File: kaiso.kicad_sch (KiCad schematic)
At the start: 413 parts, among them J1 JST_SH_Conn_01x04, J2 Conn_01x04_Pin, J4 Conn_01x02, SW0_0 Mechanical_Switch, SW0_1 Mechanical_Switch, SW0_10 Mechanical_Switch, SW0_11 Mechanical_Switch, SW0_12 Mechanical_Switch, SW0_13 Mechanical_Switch, SW0_14 Mechanical_Switch, SW0_15 Mechanical_Switch, SW0_16 Mechanical_Switch, SW0_17 Mechanical_Switch, SW0_2 Mechanical_Switch, SW0_3 Mechanical_Switch, SW0_4 Mechanical_Switch, SW0_5 Mechanical_Switch, SW0_6 Mechanical_Switch, SW0_7 Mechanical_Switch, SW0_8 Mechanical_Switch, SW0_9 Mechanical_Switch, SW1 SW_SPDT, SW1_0 Mechanical_Switch, SW1_1 Mechanical_Switch, SW1_10 Mechanical_Switch, SW1_11 Mechanical_Switch, SW1_12 Mechanical_Switch, SW1_13 Mechanical_Switch, SW1_15 Mechanical_Switch, SW1_16 Mechanical_Switch, SW1_17 Mechanical_Switch, SW1_2 Mechanical_Switch, SW1_3 Mechanical_Switch, SW1_4 Mechanical_Switch, SW1_5 Mechanical_Switch, SW1_6 Mechanical_Switch, SW1_7 Mechanical_Switch, SW1_8 Mechanical_Switch, SW1_9 Mechanical_Switch, SW2_0 Mechanical_Switch, SW2_1 Mechanical_Switch, SW2_10 Mechanical_Switch, SW2_11 Mechanical_Switch, SW2_12 Mechanical_Switch, SW2_13 Mechanical_Switch, SW2_15 Mechanical_Switch, SW2_16 Mechanical_Switch, SW2_17 Mechanical_Switch, SW2_2 Mechanical_Switch, SW2_3 Mechanical_Switch, SW2_4 Mechanical_Switch, SW2_5 Mechanical_Switch, SW2_6 Mechanical_Switch, SW2_7 Mechanical_Switch, SW2_8 Mechanical_Switch, SW2_9 Mechanical_Switch, SW3_0 Mechanical_Switch, SW3_1 Mechanical_Switch, SW3_10 Mechanical_Switch, SW3_11 Mechanical_Switch, SW3_12 Mechanical_Switch, SW3_15 Mechanical_Switch, SW3_16 Mechanical_Switch, SW3_17 Mechanical_Switch, SW3_2 Mechanical_Switch, SW3_3 Mechanical_Switch, SW3_4 Mechanical_Switch, SW3_5 Mechanical_Switch, SW3_6 Mechanical_Switch, SW3_7 Mechanical_Switch, SW3_8 Mechanical_Switch, SW3_9 Mechanical_Switch, SW4_0 Mechanical_Switch, SW4_1 Mechanical_Switch, SW4_10 Mechanical_Switch, SW4_11 Mechanical_Switch, SW4_12 Mechanical_Switch, SW4_15 Mechanical_Switch, SW4_16 Mechanical_Switch, SW4_17 Mechanical_Switch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

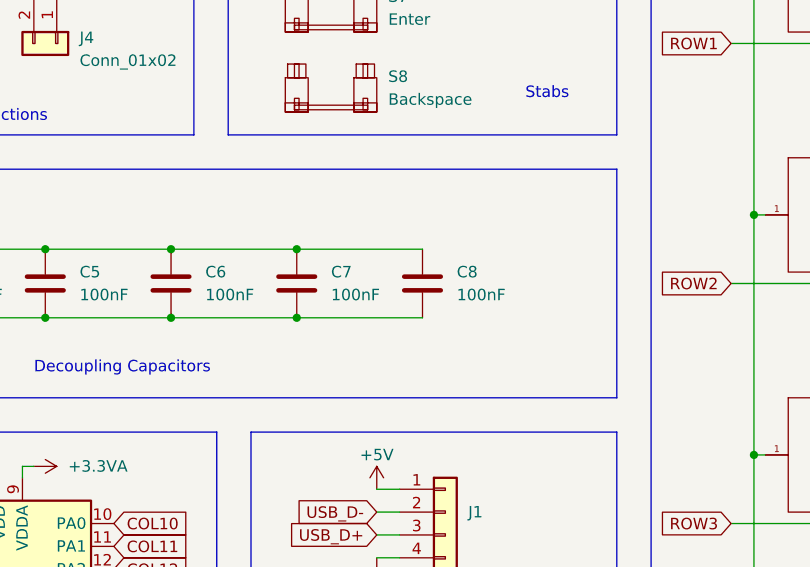
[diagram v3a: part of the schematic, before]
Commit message: started the PCB design
layout complete with switches. still need to figure out how to route it.
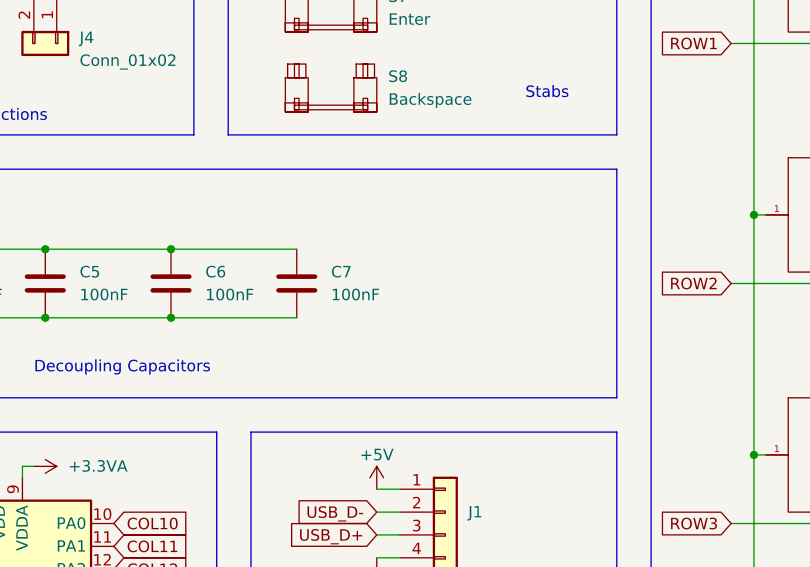
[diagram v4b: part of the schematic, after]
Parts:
- removed C8: 100nF, Capacitor_SMD:C_0402_1005Metric, symbol Device:C
- J1: footprint Connector_JST:JST_SH_BM04B-SRSS-TB_1x04-1MP_P1.00mm_Vertical -> Connector_JST:JST_SH_SM04B-SRSS-TB_1x04-1MP_P1.00mm_Horizontal
- SW1: footprint SW:SW-TH_SK12D07VG3 -> Button_Switch_SMD:SW_SPDT_PCM12
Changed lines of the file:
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@@
   (junction (at 251.46 76.2) (diameter 0) (color 0 0 0 0)
   )
-  (junction (at 81.28 300.99) (diameter 0) (color 0 0 0 0)
-  )
   (junction (at 267.97 163.83) (diameter 0) (color 0 0 0 0)
   )
@@
   (junction (at 135.89 88.9) (diameter 0) (color 0 0 0 0)
   )
-  (junction (at 81.28 293.37) (diameter 0) (color 0 0 0 0)
-  )
   (junction (at 234.95 105.41) (diameter 0) (color 0 0 0 0)
   )
@@
     (stroke (width 0) (type default))
   )
-  (wire (pts (xy 81.28 293.37) (xy 95.25 293.37))
-    (stroke (width 0) (type default))
-  )
   (wire (pts (xy 128.27 97.79) (xy 124.46 97.79))
     (stroke (width 0) (type default))
@@
     (stroke (width 0) (type default))
   )
-  (wire (pts (xy 81.28 300.99) (xy 95.25 300.99))
-    (stroke (width 0) (type default))
-  )
   (wire (pts (xy 248.92 243.84) (xy 266.7 243.84))
     (stroke (width 0) (type default))
@@
       (effects (font (size 1.27 1.27)) (justify left))
     )
-    (property "Footprint" "Connector_JST:JST_SH_BM04B-SRSS-TB_1x04-1MP_P1.00mm_Vertical" (at 97.79 322.58 0)
+    (property "Footprint" "Connector_JST:JST_SH_SM04B-SRSS-TB_1x04-1MP_P1.00mm_Horizontal" (at 97.79 322.58 0)
       (effects (font (size 1.27 1.27)) hide)
     )
@@
     )
   )
-  (symbol (lib_id "Device:C") (at 95.25 297.18 0) (unit 1)
-    (in_bom yes) (on_board yes) (dnp no) (fields_autoplaced)
-    (property "Reference" "C8" (at 99.06 295.91 0)
-      (effects (font (size 1.27 1.27)) (justify left))
-    )
-    (property "Value" "100nF" (at 99.06 298.45 0)
-      (effects (font (size 1.27 1.27)) (justify left))
-    )
-    (property "Footprint" "Capacitor_SMD:C_0402_1005Metric" (at 96.2152 300.99 0)
-      (effects (font (size 1.27 1.27)) hide)
-    )
-    (property "Datasheet" "~" (at 95.25 297.18 0)
-      (effects (font (size 1.27 1.27)) hide)
-    )
-    (pin "1")
-    (pin "2")
-    (instances
-      (project "kaiso"
-        (path "/736a7f90-df3f-4c7b-84f9-639d23f495c2"
-          (reference "C8") (unit 1)
-        )
-      )
-    )
-  )
   (symbol (lib_id "PCM_marbastlib-mx:MX_SK6812MINI-E") (at 400.05 97.79 0) (unit 1)
     (in_bom yes) (on_board yes) (dnp no)
@@
       (effects (font (size 1.27 1.27)))
     )
-    (property "Footprint" "SW:SW-TH_SK12D07VG3" (at 34.29 255.27 0)
+    (property "Footprint" "Button_Switch_SMD:SW_SPDT_PCM12" (at 34.29 255.27 0)
       (effects (font (size 1.27 1.27)) hide)
     )
